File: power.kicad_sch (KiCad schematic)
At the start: 52 parts, among them J4 Conn_01x02, Q1 Q_NMOS, Q2 Q_NMOS, U2 LDL212PVR, U3 LDL212PVR, U5 LDL212PVR, U6 LDL212PVR, U8 TPS62933O, U9 LM74502

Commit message: schem: reannotate
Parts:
- renumbered C1 to C44, C2 to C45, C3 to C46, C59 to C47, C55 to C48, C60 to C49, C56 to C50, C57 to C51, C58 to C52, C61 to C53, C30 to C54, C10 to C55, C6 to C56, C22 to C57, C31 to C58, C11 to C59, C9 to C60, C23 to C61, D6 to D12, D10 to D13, D9 to D14, J4 to J8, JP3 to JP1, R13 to R36, R30 to R37, R31 to R38, R10 to R39, R12 to R40, R4 to R41, R25 to R42, R3 to R43, R22 to R44, R20 to R45, R21 to R46, R23 to R47, R24 to R48, TP2 to TP14, TP9 to TP15, TP7 to TP16, TP4 to TP17, TP6 to TP18, TP3 to TP19, U5 to U10, U8 to U5, U9 to U6, U6 to U7, U3 to U8, U2 to U9

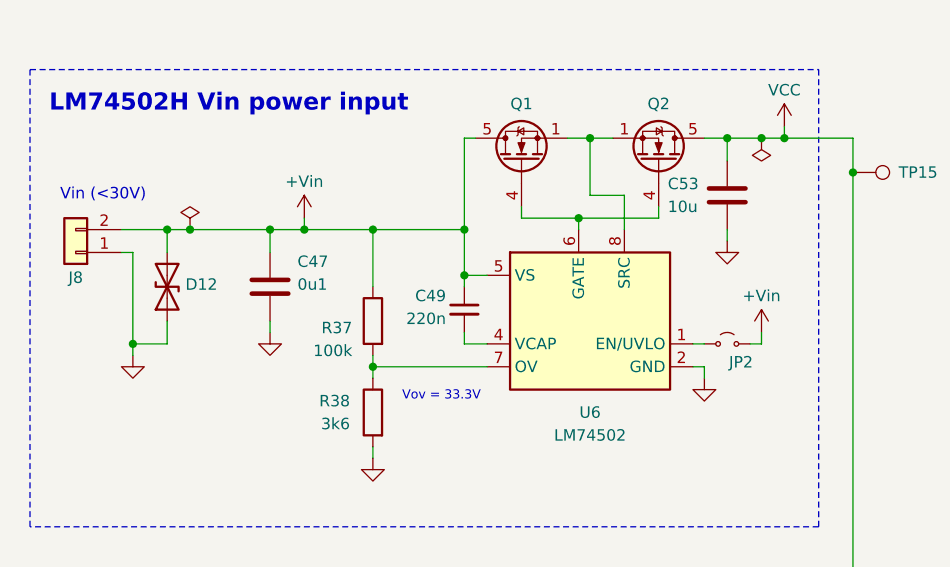
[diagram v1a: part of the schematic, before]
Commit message: schem: switch load switch to always on
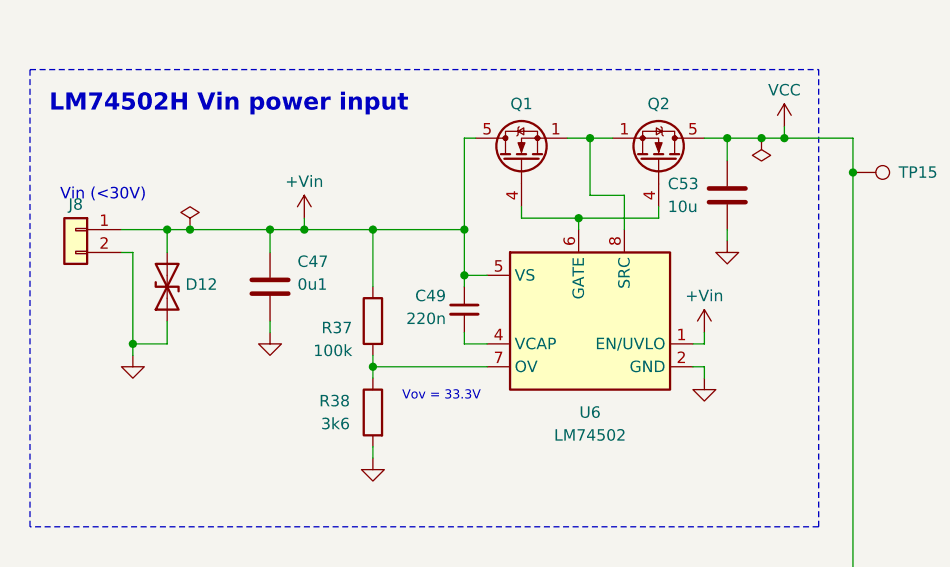
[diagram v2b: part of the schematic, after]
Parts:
- removed JP2: Jumper_2_Small_Open, Connector_PinHeader_2.54mm:PinHeader_1x02_P2.54mm_Vertical, symbol Jumper:Jumper_2_Small_Open
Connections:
- net +Vin: now also J8.1 (Pin_1), U6.1 (EN/UVLO); no longer J8.2 (Pin_2)
- net GND: now also J8.2 (Pin_2); no longer J8.1 (Pin_1)
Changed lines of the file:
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@@
 	(wire
 		(pts
-			(xy 134.62 71.12) (xy 134.62 72.39)
+			(xy 128.27 71.12) (xy 128.27 72.39)
 		)
 		(stroke
@@
 	(wire
 		(pts
-			(xy 133.35 72.39) (xy 134.62 72.39)
-		)
-		(stroke
-			(width 0)
-			(type default)
-		)
-	)
-	(wire
-		(pts
 			(xy 72.39 110.49) (xy 72.39 111.76)
 		)
@@
 	(symbol
 		(lib_id "power:VCC")
-		(at 134.62 71.12 0)
+		(at 128.27 71.12 0)
 		(unit 1)
 		(body_style 1)
@@
 		(dnp no)
 		(property "Reference" "#PWR099"
-			(at 134.62 74.93 0)
+			(at 128.27 74.93 0)
 			(hide yes)
 			(show_name no)
@@
 		)
 		(property "Value" "+Vin"
-			(at 134.62 67.056 0)
+			(at 128.27 67.056 0)
 			(show_name no)
 			(do_not_autoplace no)
@@
 		)
 		(property "Footprint" ""
-			(at 134.62 71.12 0)
+			(at 128.27 71.12 0)
 			(hide yes)
 			(show_name no)
@@
 		)
 		(property "Datasheet" ""
-			(at 134.62 71.12 0)
+			(at 128.27 71.12 0)
 			(hide yes)
 			(show_name no)
@@
 		)
 		(property "Description" "Power symbol creates a global label with name \"VCC\""
-			(at 134.62 71.12 0)
+			(at 128.27 71.12 0)
 			(hide yes)
 			(show_name no)
@@
 	)
 	(symbol
-		(lib_id "Jumper:Jumper_2_Small_Open")
-		(at 130.81 72.39 0)
-		(unit 1)
-		(body_style 1)
-		(exclude_from_sim no)
-		(in_bom no)
-		(on_board yes)
-		(in_pos_files yes)
-		(dnp no)
-		(property "Reference" "JP2"
-			(at 132.334 74.422 0)
-			(show_name no)
-			(do_not_autoplace no)
-			(effects
-				(font
-					(size 1.27 1.27)
-				)
-			)
-		)
-		(property "Value" "Jumper_2_Small_Open"
-			(at 129.5401 73.66 90)
-			(hide yes)
-			(show_name no)
-			(do_not_autoplace no)
-			(effects
-				(font
-					(size 1.27 1.27)
-				)
-				(justify right)
-			)
-		)
-		(property "Footprint" "Connector_PinHeader_2.54mm:PinHeader_1x02_P2.54mm_Vertical"
-			(at 130.81 72.39 0)
-			(hide yes)
-			(show_name no)
-			(do_not_autoplace no)
-			(effects
-				(font
-					(size 1.27 1.27)
-				)
-			)
-		)
-		(property "Datasheet" ""
-			(at 130.81 72.39 0)
-			(hide yes)
-			(show_name no)
-			(do_not_autoplace no)
-			(effects
-				(font
-					(size 1.27 1.27)
-				)
-			)
-		)
-		(property "Description" "Jumper, 2-pole, small symbol, open"
-			(at 130.81 72.39 0)
-			(hide yes)
-			(show_name no)
-			(do_not_autoplace no)
-			(effects
-				(font
-					(size 1.27 1.27)
-				)
-			)
-		)
-		(pin "2"
-		)
-		(pin "1"
-		)
-		(instances
-			(project "s6tm-stereo-dev-1"
-				(path "/41fad0d7-0cae-453e-a16c-bdf8be036e99/16b0527c-413f-47f6-bff3-a7959715851d"
-					(reference "JP2")
-					(unit 1)
-				)
-			)
-		)
-	)
-	(symbol
-		(lib_id "Connector_Generic:Conn_01x02")
-		(at 58.42 62.23 180)
-		(unit 1)
-		(body_style 1)
-		(exclude_from_sim no)
-		(in_bom no)
-		(on_board yes)
-		(in_pos_files yes)
-		(dnp no)
-		(property "Reference" "J8"
-			(at 58.42 65.024 0)
-			(show_name no)
-			(do_not_autoplace no)
-			(effects
-				(font
-					(size 1.27 1.27)
-				)
-			)
-		)
-		(property "Value" "Conn_01x02"
-			(at 58.42 55.88 0)
-			(hide yes)
-			(show_name no)
-			(do_not_autoplace no)
-			(effects
-				(font
-					(size 1.27 1.27)
-				)
-			)
-		)
-		(property "Footprint" "TerminalBlock_Phoenix:TerminalBlock_Phoenix_MKDS-1,5-2-5.08_1x02_P5.08mm_Horizontal"
-			(at 58.42 62.23 0)
-			(hide yes)
-			(show_name no)
-			(do_not_autoplace no)
-			(effects
-				(font
-					(size 1.27 1.27)
-				)
-			)
-		)
-		(property "Datasheet" ""
-			(at 58.42 62.23 0)
-			(hide yes)
-			(show_name no)
-			(do_not_autoplace no)
-			(effects
-				(font
-					(size 1.27 1.27)
-				)
-			)
-		)
-		(property "Description" "Generic connector, single row, 01x02, script generated (kicad-library-utils/schlib/autogen/connector/)"
-			(at 58.42 62.23 0)
-			(hide yes)
-			(show_name no)
-			(do_not_autoplace no)
-			(effects
-				(font
-					(size 1.27 1.27)
-				)
-			)
-		)
-		(pin "1"
-		)
-		(pin "2"
-		)
-		(instances
-			(project "s6tm-stereo-dev-1"
-				(path "/41fad0d7-0cae-453e-a16c-bdf8be036e99/16b0527c-413f-47f6-bff3-a7959715851d"
-					(reference "J8")
-					(unit 1)
-				)
-			)
-		)
-	)
-	(symbol
 		(lib_id "Device:C")
 		(at 237.49 137.16 0)
@@
 					(unit 1)
 				)
+			)
+		)
+	)
+	(symbol
+		(lib_id "Connector_Generic:Conn_01x02")
+		(at 58.42 59.69 0)
+		(mirror y)
+		(unit 1)
+		(body_style 1)
+		(exclude_from_sim no)
+		(in_bom no)
+		(on_board yes)
+		(in_pos_files yes)
+		(dnp no)
+		(property "Reference" "J8"
+			(at 58.42 56.896 0)
+			(show_name no)
+			(do_not_autoplace no)
+			(effects
+				(font
+					(size 1.27 1.27)
+				)
+			)
+		)
+		(property "Value" "Conn_01x02"
+			(at 58.42 66.04 0)
+			(hide yes)
+			(show_name no)
+			(do_not_autoplace no)
+			(effects
+				(font
+					(size 1.27 1.27)
+				)
+			)
+		)
+		(property "Footprint" "TerminalBlock_Phoenix:TerminalBlock_Phoenix_MKDS-1,5-2-5.08_1x02_P5.08mm_Horizontal"
+			(at 58.42 59.69 0)
+			(hide yes)
+			(show_name no)
+			(do_not_autoplace no)
+			(effects
+				(font
+					(size 1.27 1.27)
+				)
+			)
+		)
+		(property "Datasheet" ""
+			(at 58.42 59.69 0)
+			(hide yes)
+			(show_name no)
+			(do_not_autoplace no)
+			(effects
+				(font
+					(size 1.27 1.27)
+				)
+			)
+		)
+		(property "Description" "Generic connector, single row, 01x02, script generated (kicad-library-utils/schlib/autogen/connector/)"
+			(at 58.42 59.69 0)
+			(hide yes)
+			(show_name no)
+			(do_not_autoplace no)
+			(effects
+				(font
+					(size 1.27 1.27)
+				)
+			)
+		)
+		(pin "1"
+		)
+		(pin "2"
+		)
+		(instances
+			(project "s6tm-stereo-dev-1"
+				(path "/41fad0d7-0cae-453e-a16c-bdf8be036e99/16b0527c-413f-47f6-bff3-a7959715851d"
+					(reference "J8")
+					(unit 1)
+				)

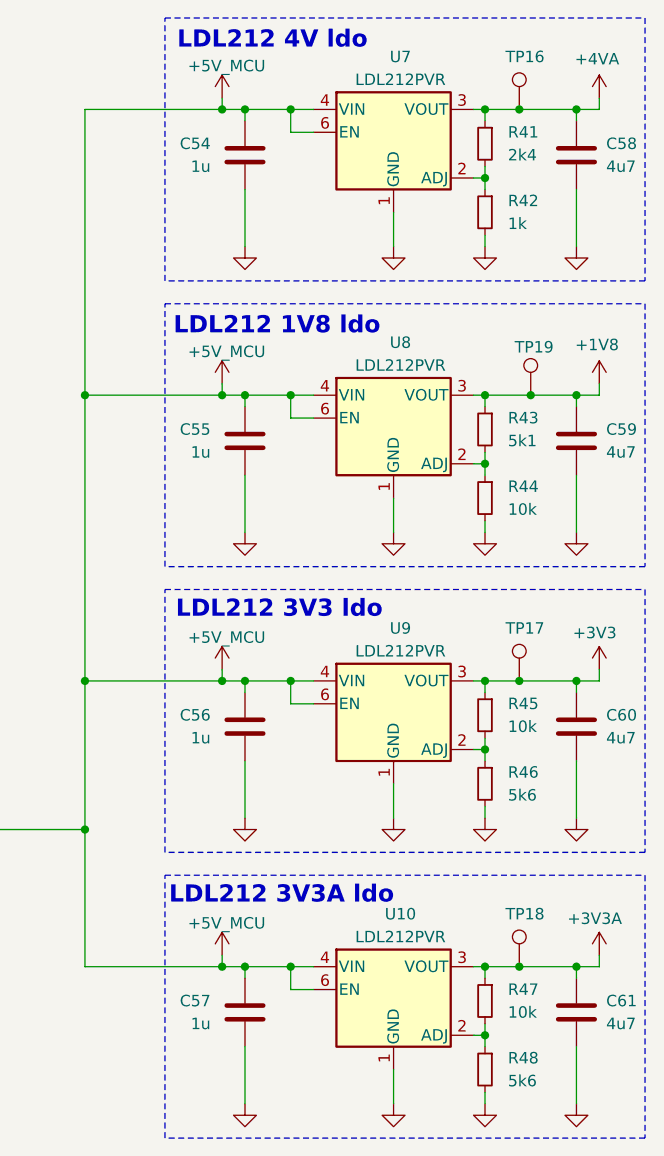
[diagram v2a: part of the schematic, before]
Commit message: pcb: add LDOs layout
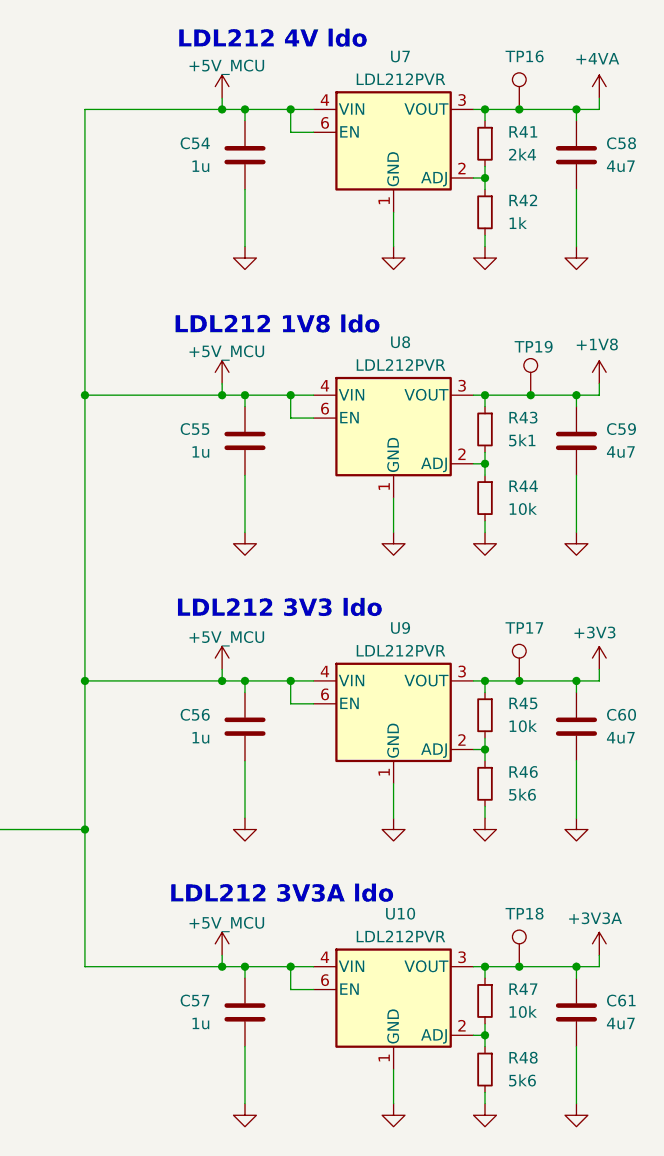
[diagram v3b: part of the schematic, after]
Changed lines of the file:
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@@
-	)
-	(rectangle
-		(start 191.77 26.67)
-		(end 245.11 55.88)
-		(stroke
-			(width 0)
-			(type dash)
-		)
-		(fill
-			(type none)
-		)
-	)
-	(rectangle
-		(start 191.77 121.92)
-		(end 245.11 151.13)
-		(stroke
-			(width 0)
-			(type dash)
-		)
-		(fill
-			(type none)
-		)
 	)
 	(rectangle
 		(start 53.34 41.91)
 		(end 140.97 92.71)
-		(stroke
-			(width 0)
-			(type dash)
-		)
-		(fill
-			(type none)
-		)
-	)
-	(rectangle
-		(start 191.77 90.17)
-		(end 245.11 119.38)
-		(stroke
-			(width 0)
-			(type dash)
-		)
-		(fill
-			(type none)
-		)
-	)
-	(rectangle
-		(start 191.77 58.42)
-		(end 245.11 87.63)
 		(stroke
 			(width 0)
@@
 		)
 	)
+	(rule_area
+		(exclude_from_sim no)
+		(in_bom yes)
+		(on_board yes)
+		(dnp no)
+		(polyline
+			(pts
+				(xy 191.77 26.67) (xy 245.11 26.67) (xy 245.11 55.88) (xy 191.77 55.88)
+			)
+			(stroke
+				(width 0)
+				(type dash)
+			)
+			(fill
+				(type none)
+			)
+		)
+	)
+	(rule_area
+		(exclude_from_sim no)
+		(in_bom yes)
+		(on_board yes)
+		(dnp no)
+		(polyline
+			(pts
+				(xy 191.77 121.92) (xy 245.11 121.92) (xy 245.11 151.13) (xy 191.77 151.13)
+			)
+			(stroke
+				(width 0)
+				(type dash)
+			)
+			(fill
+				(type none)
+			)
+		)
+	)
+	(rule_area
+		(exclude_from_sim no)
+		(in_bom yes)
+		(on_board yes)
+		(dnp no)
+		(polyline
+			(pts
+				(xy 191.77 58.42) (xy 245.11 58.42) (xy 245.11 87.63) (xy 191.77 87.63)
+			)
+			(stroke
+				(width 0)
+				(type dash)
+			)
+			(fill
+				(type none)
+			)
+		)
+	)
+	(rule_area
+		(exclude_from_sim no)
+		(in_bom yes)
+		(on_board yes)
+		(dnp no)
+		(polyline
+			(pts
+				(xy 191.77 90.17) (xy 245.11 90.17) (xy 245.11 119.38) (xy 191.77 119.38)
+			)
+			(stroke
+				(width 0)
+				(type dash)
+			)
+			(fill
+				(type none)
+			)
+		)
+	)
+	(netclass_flag ""
+		(length 2.54)
+		(shape round)
+		(at 191.77 27.94 90)
+		(effects
+			(font
+				(size 1.27 1.27)
+			)
+			(justify left bottom)
+		)
+		(property "Net Class" ""
+			(at -90.17 13.97 0)
+			(show_name no)
+			(do_not_autoplace no)
+			(effects
+				(font
+					(size 1.27 1.27)
+				)
+			)
+		)
+		(property "Component Class" "LDO_4V"
+			(at 184.15 25.908 0)
+			(show_name no)
+			(do_not_autoplace no)
+			(effects
+				(font
+					(size 1.27 1.27)
+					(italic yes)
+				)
+				(justify left)
+			)
+		)
+	)
+	(netclass_flag ""
+		(length 2.54)
+		(shape round)
+		(at 191.77 91.44 90)
+		(effects
+			(font
+				(size 1.27 1.27)
+			)
+			(justify left bottom)
+		)
+		(property "Net Class" ""
+			(at -90.17 77.47 0)
+			(show_name no)
+			(do_not_autoplace no)
+			(effects
+				(font
+					(size 1.27 1.27)
+				)
+			)
+		)
+		(property "Component Class" "LDO_3V3"
+			(at 183.388 89.662 0)
+			(show_name no)
+			(do_not_autoplace no)
+			(effects
+				(font
+					(size 1.27 1.27)
+					(italic yes)
+				)
+				(justify left)
+			)
+		)
+	)
+	(netclass_flag ""
+		(length 2.54)
+		(shape round)
+		(at 191.77 59.69 90)
+		(effects
+			(font
+				(size 1.27 1.27)
+			)
+			(justify left bottom)
+		)
+		(property "Net Class" ""
+			(at -90.17 45.72 0)
+			(show_name no)
+			(do_not_autoplace no)
+			(effects
+				(font
+					(size 1.27 1.27)
+				)
+			)
+		)
+		(property "Component Class" "LDO_1V8"
+			(at 183.388 57.912 0)
+			(show_name no)
+			(do_not_autoplace no)
+			(effects
+				(font
+					(size 1.27 1.27)
+					(italic yes)
+				)
+				(justify left)
+			)
+		)
+	)
+	(netclass_flag ""
+		(length 2.54)
+		(shape round)
+		(at 191.77 123.19 90)
+		(effects
+			(font
+				(size 1.27 1.27)
+			)
+			(justify left bottom)
+		)
+		(property "Net Class" ""
+			(at -90.17 109.22 0)
+			(show_name no)
+			(do_not_autoplace no)
+			(effects
+				(font
+					(size 1.27 1.27)
+				)
+			)
+		)
+		(property "Component Class" "LDO_3V3A"
+			(at 183.388 120.904 0)
+			(show_name no)
+			(do_not_autoplace no)
+			(effects
+				(font
+					(size 1.27 1.27)
+					(italic yes)
+				)
+				(justify left)
+			)
+		)
+	)

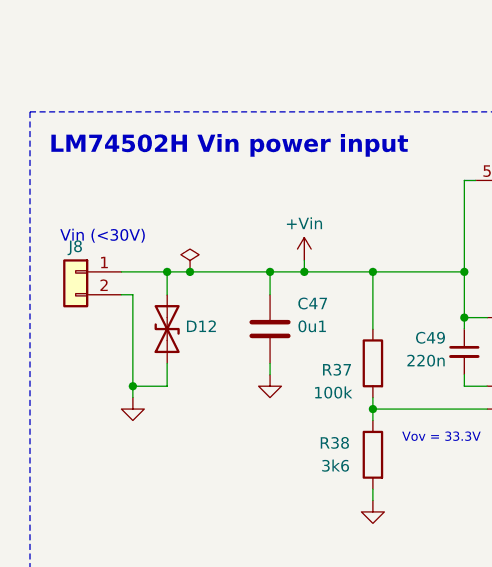
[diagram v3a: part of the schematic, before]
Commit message: pcb: rpp and smps layout refinement
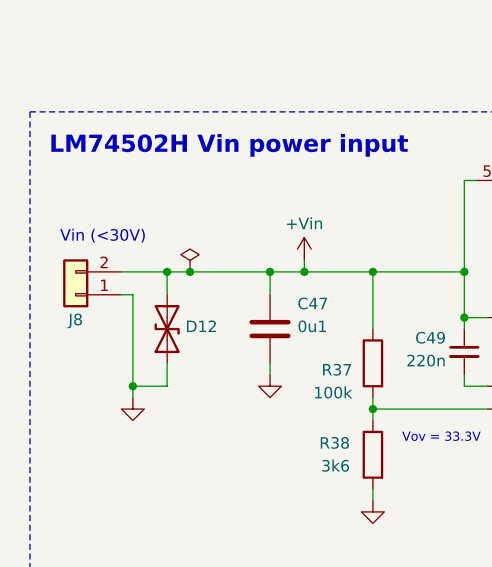
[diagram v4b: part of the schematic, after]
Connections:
- net +Vin: now also J8.2 (Pin_2); no longer J8.1 (Pin_1)
- net GND: now also J8.1 (Pin_1); no longer J8.2 (Pin_2)
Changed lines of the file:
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@@
+	)
+	(symbol
+		(lib_id "Connector_Generic:Conn_01x02")
+		(at 58.42 62.23 180)
+		(unit 1)
+		(body_style 1)
+		(exclude_from_sim no)
+		(in_bom no)
+		(on_board yes)
+		(in_pos_files yes)
+		(dnp no)
+		(property "Reference" "J8"
+			(at 58.42 65.024 0)
+			(show_name no)
+			(do_not_autoplace no)
+			(effects
+				(font
+					(size 1.27 1.27)
+				)
+			)
+		)
+		(property "Value" "Conn_01x02"
+			(at 58.42 55.88 0)
+			(hide yes)
+			(show_name no)
+			(do_not_autoplace no)
+			(effects
+				(font
+					(size 1.27 1.27)
+				)
+			)
+		)
+		(property "Footprint" "TerminalBlock_Phoenix:TerminalBlock_Phoenix_MKDS-1,5-2-5.08_1x02_P5.08mm_Horizontal"
+			(at 58.42 62.23 0)
+			(hide yes)
+			(show_name no)
+			(do_not_autoplace no)
+			(effects
+				(font
+					(size 1.27 1.27)
+				)
+			)
+		)
+		(property "Datasheet" ""
+			(at 58.42 62.23 0)
+			(hide yes)
+			(show_name no)
+			(do_not_autoplace no)
+			(effects
+				(font
+					(size 1.27 1.27)
+				)
+			)
+		)
+		(property "Description" "Generic connector, single row, 01x02, script generated (kicad-library-utils/schlib/autogen/connector/)"
+			(at 58.42 62.23 0)
+			(hide yes)
+			(show_name no)
+			(do_not_autoplace no)
+			(effects
+				(font
+					(size 1.27 1.27)
+				)
+			)
+		)
+		(pin "1"
+		)
+		(pin "2"
+		)
+		(instances
+			(project "s6tm-stereo-dev-1"
+				(path "/41fad0d7-0cae-453e-a16c-bdf8be036e99/16b0527c-413f-47f6-bff3-a7959715851d"
+					(reference "J8")
+					(unit 1)
+				)
+			)
+		)
 	)
 	(symbol
@@
 					(unit 1)
 				)
-			)
-		)
-	)
-	(symbol
-		(lib_id "Connector_Generic:Conn_01x02")
-		(at 58.42 59.69 0)
-		(mirror y)
-		(unit 1)
-		(body_style 1)
-		(exclude_from_sim no)
-		(in_bom no)
-		(on_board yes)
-		(in_pos_files yes)
-		(dnp no)
-		(property "Reference" "J8"
-			(at 58.42 56.896 0)
-			(show_name no)
-			(do_not_autoplace no)
-			(effects
-				(font
-					(size 1.27 1.27)
-				)
-			)
-		)
-		(property "Value" "Conn_01x02"
-			(at 58.42 66.04 0)
-			(hide yes)
-			(show_name no)
-			(do_not_autoplace no)
-			(effects
-				(font
-					(size 1.27 1.27)
-				)
-			)
-		)
-		(property "Footprint" "TerminalBlock_Phoenix:TerminalBlock_Phoenix_MKDS-1,5-2-5.08_1x02_P5.08mm_Horizontal"
-			(at 58.42 59.69 0)
-			(hide yes)
-			(show_name no)
-			(do_not_autoplace no)
-			(effects
-				(font
-					(size 1.27 1.27)
-				)
-			)
-		)
-		(property "Datasheet" ""
-			(at 58.42 59.69 0)
-			(hide yes)
-			(show_name no)
-			(do_not_autoplace no)
-			(effects
-				(font
-					(size 1.27 1.27)
-				)
-			)
-		)
-		(property "Description" "Generic connector, single row, 01x02, script generated (kicad-library-utils/schlib/autogen/connector/)"
-			(at 58.42 59.69 0)
-			(hide yes)
-			(show_name no)
-			(do_not_autoplace no)
-			(effects
-				(font
-					(size 1.27 1.27)
-				)
-			)
-		)
-		(pin "1"
-		)
-		(pin "2"
-		)
-		(instances
-			(project "s6tm-stereo-dev-1"
-				(path "/41fad0d7-0cae-453e-a16c-bdf8be036e99/16b0527c-413f-47f6-bff3-a7959715851d"
-					(reference "J8")
-					(unit 1)
-				)

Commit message: pcb: add audio layout
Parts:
- removed TP15: TestPoint, TestPoint:TestPoint_Pad_D2.0mm, symbol Connector:TestPoint
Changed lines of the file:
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@@
 	)
 	(junction
-		(at 144.78 53.34)
-		(diameter 0)
-		(color 0 0 0 0)
-	)
-	(junction
 		(at 59.69 110.49)
 		(diameter 0)
@@
 	(wire
 		(pts
-			(xy 144.78 49.53) (xy 144.78 53.34)
+			(xy 144.78 49.53) (xy 144.78 97.79)
 		)
 		(stroke
@@
 	(wire
 		(pts
-			(xy 144.78 53.34) (xy 144.78 97.79)
-		)
-		(stroke
-			(width 0)
-			(type default)
-		)
-	)
-	(wire
-		(pts
 			(xy 208.28 68.58) (xy 205.74 68.58)
 		)
@@
 					(unit 1)
 				)
-			)
-		)
-	)
-	(symbol
-		(lib_id "Connector:TestPoint")
-		(at 144.78 53.34 270)
-		(unit 1)
-		(body_style 1)
-		(exclude_from_sim no)
-		(in_bom no)
-		(on_board yes)
-		(in_pos_files yes)
-		(dnp no)
-		(fields_autoplaced yes)
-		(property "Reference" "TP15"
-			(at 149.86 53.3399 90)
-			(show_name no)
-			(do_not_autoplace no)
-			(effects
-				(font
-					(size 1.27 1.27)
-				)
-				(justify left)
-			)
-		)
-		(property "Value" "TestPoint"
-			(at 146.8121 55.88 0)
-			(hide yes)
-			(show_name no)
-			(do_not_autoplace no)
-			(effects
-				(font
-					(size 1.27 1.27)
-				)
-				(justify left)
-			)
-		)
-		(property "Footprint" "TestPoint:TestPoint_Pad_D2.0mm"
-			(at 144.78 58.42 0)
-			(hide yes)
-			(show_name no)
-			(do_not_autoplace no)
-			(effects
-				(font
-					(size 1.27 1.27)
-				)
-			)
-		)
-		(property "Datasheet" ""
-			(at 144.78 58.42 0)
-			(hide yes)
-			(show_name no)
-			(do_not_autoplace no)
-			(effects
-				(font
-					(size 1.27 1.27)
-				)
-			)
-		)
-		(property "Description" "test point"
-			(at 144.78 53.34 0)
-			(hide yes)
-			(show_name no)
-			(do_not_autoplace no)
-			(effects
-				(font
-					(size 1.27 1.27)
-				)
-			)
-		)
-		(pin "1"
-		)
-		(instances
-			(project "s6tm-stereo-dev-1"
-				(path "/41fad0d7-0cae-453e-a16c-bdf8be036e99/16b0527c-413f-47f6-bff3-a7959715851d"
-					(reference "TP15")
-					(unit 1)
-				)
